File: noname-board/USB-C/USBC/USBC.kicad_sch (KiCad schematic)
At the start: 10 parts, among them J2 USB_C_Receptacle, U4 AP2112K-3.3

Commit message: GPIO
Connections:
- net USB_DM renamed USB_D-
- net USB_DP renamed USB_D+
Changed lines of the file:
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@@
     )
   )
-  (hierarchical_label "USB_DP" (shape input) (at 81.28 54.61 270) (fields_autoplaced)
+  (hierarchical_label "USB_D+" (shape input) (at 81.28 54.61 270) (fields_autoplaced)
     (effects (font (size 1.27 1.27)) (justify right))
   )
-  (hierarchical_label "USB_DM" (shape input) (at 85.09 48.26 270) (fields_autoplaced)
+  (hierarchical_label "USB_D-" (shape input) (at 85.09 48.26 270) (fields_autoplaced)
     (effects (font (size 1.27 1.27)) (justify right))
   )

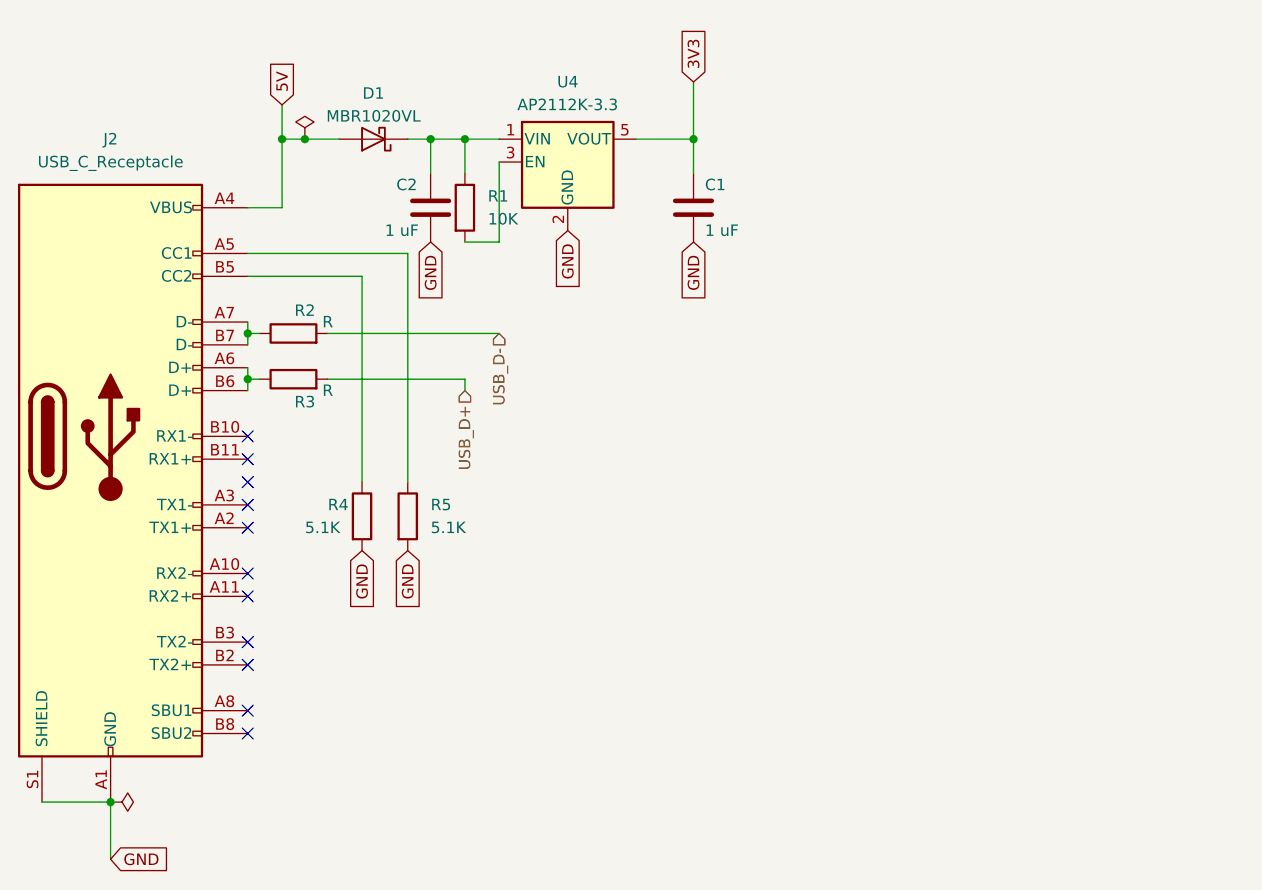
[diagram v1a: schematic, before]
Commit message: GPIO, USBC
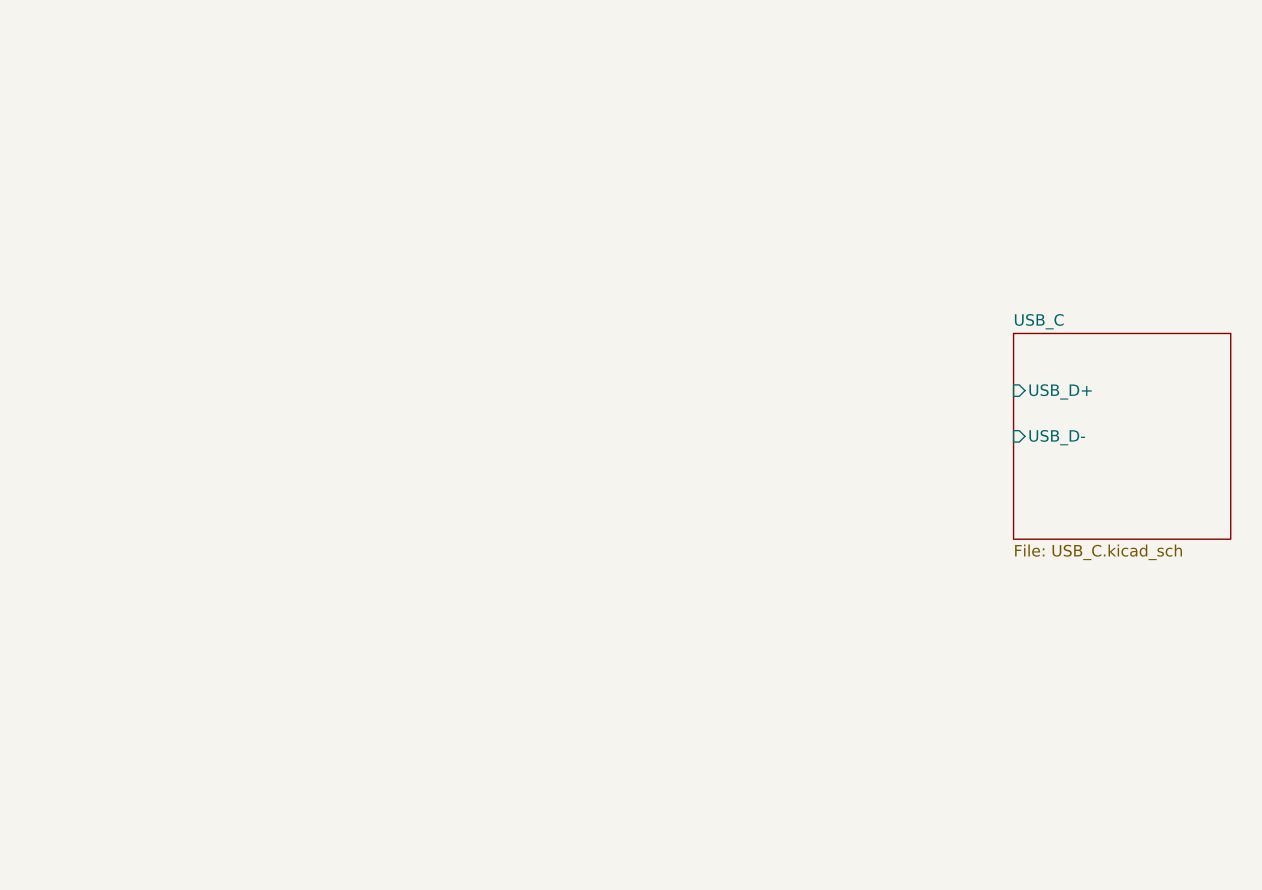
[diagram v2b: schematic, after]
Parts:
- removed C1, C2: 1 uF, symbol Device:C
- removed D1: MBR1020VL, Diode_SMD:D_SOD-123F, symbol Diode:MBR1020VL
- removed J2: USB_C_Receptacle, symbol Connector:USB_C_Receptacle
- removed R1: 10K, symbol Device:R
- removed R2, R3: R, symbol Device:R
- removed R4, R5: 5.1K, symbol Device:R
- removed U4: AP2112K-3.3, Package_TO_SOT_SMD:SOT-23-5, symbol Regulator_Linear:AP2112K-3.3
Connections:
- no-connect marks 11 -> 0
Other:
- added sheet USB_C (USB_C.kicad_sch)

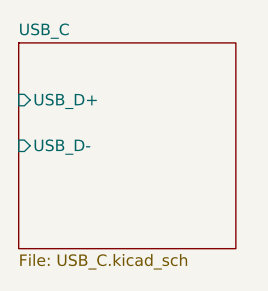
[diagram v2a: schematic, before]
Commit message: Changed Global to Hierarchals
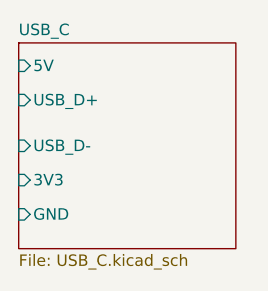
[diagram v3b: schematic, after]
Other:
- sheet USB_C ports: added 3V3, 5V, GND; removed none
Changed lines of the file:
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@@
+      (effects (font (size 1.27 1.27)) (justify left))
+    )
+    (pin "3V3" input (at 142.24 63.5 180)
+      (effects (font (size 1.27 1.27)) (justify left))
+    )
+    (pin "GND" input (at 142.24 67.31 180)
+      (effects (font (size 1.27 1.27)) (justify left))
+    )
+    (pin "5V" input (at 142.24 50.8 180)
       (effects (font (size 1.27 1.27)) (justify left))
     )
